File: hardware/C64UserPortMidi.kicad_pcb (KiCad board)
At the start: 2 copper layers, 48 x 47 mm, 13 parts, among them J1 C64-UserPort, J2 MIDI IN DIN-5, J3 AVR-ISP-6, U1 ATtiny13A-PU, U2 6N138, U3 74HC595

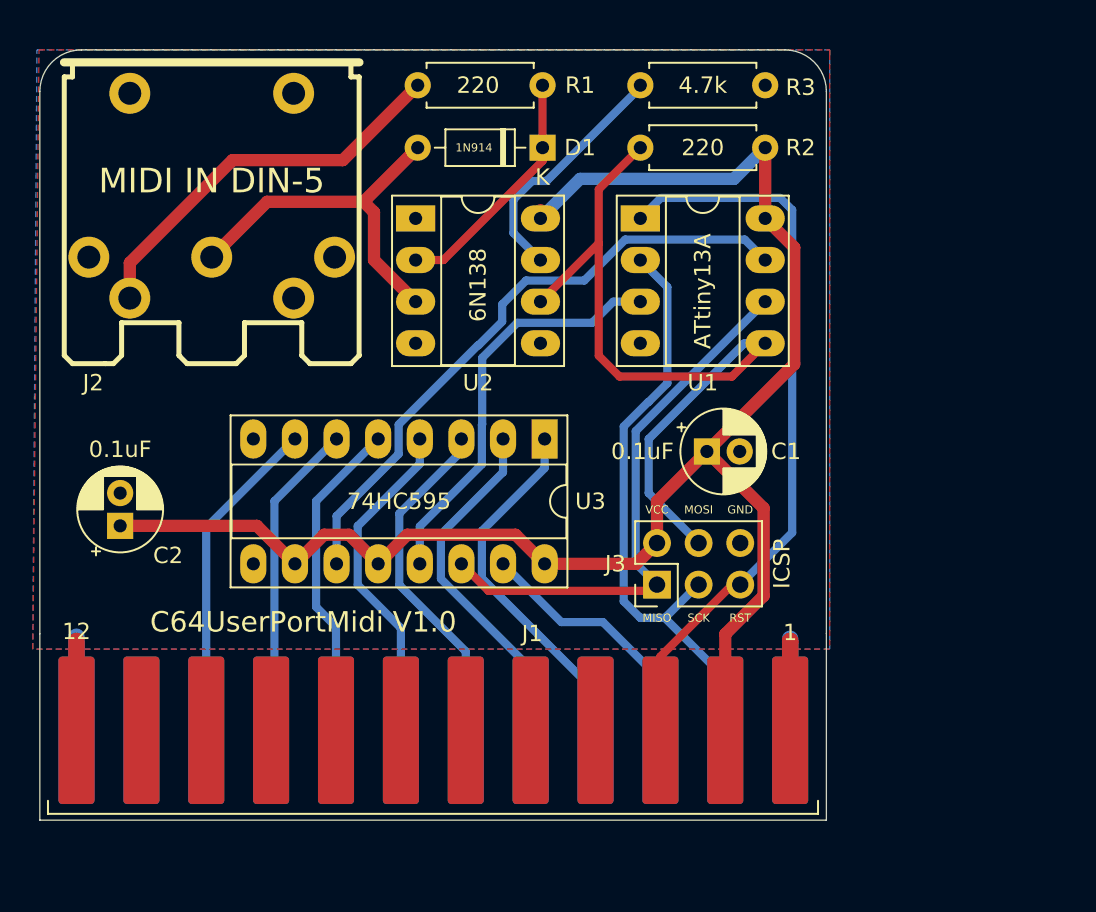
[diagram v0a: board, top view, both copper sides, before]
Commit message: Added data led and latch filtering capacitor to hardware design.
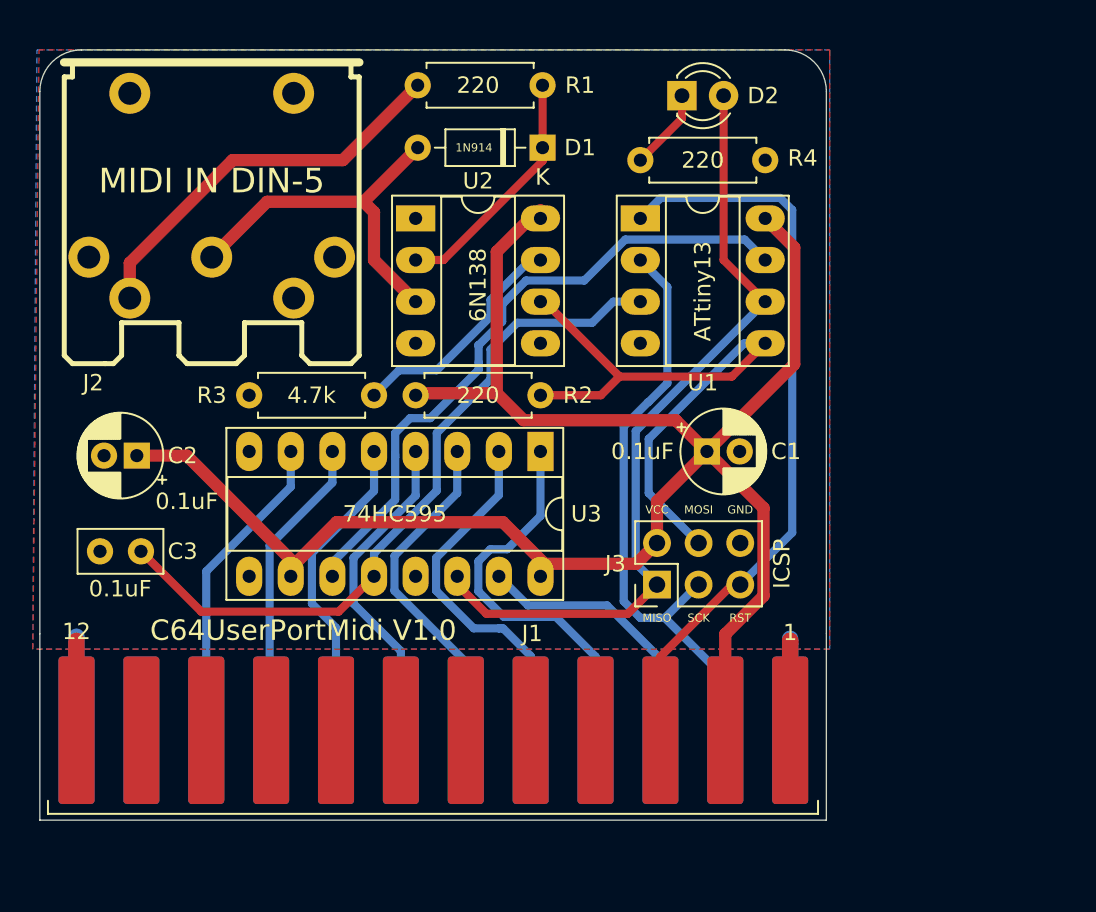
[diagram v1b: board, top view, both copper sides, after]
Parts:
- removed the REF** at (112.3, 110.0)
- added C3: 0.1uF, Capacitor_THT:C_Disc_D5.0mm_W2.5mm_P2.50mm, F.Cu at (113.0, 119.1)
- added D2: LED, LED_THT:LED_D3.0mm, F.Cu at (146.1, 91.3)
- added R4: 220, Resistor_THT:R_Axial_DIN0207_L6.3mm_D2.5mm_P7.62mm_Horizontal, F.Cu at (143.5, 95.2)
- added REF**: OSHW-Logo2_7.3x6mm_SilkScreen, Symbol:OSHW-Logo2_7.3x6mm_SilkScreen, B.Cu at (112.4, 108.8)
- moved R2 26.1 mm to (129.8, 109.6), turned to 0 degrees
- moved R3 24.9 mm to (127.3, 109.6), turned to 180 degrees
- moved C2 4.40 mm to (112.8, 113.3), turned to 180 degrees
- moved U3 0.80 mm to (137.4, 113.0)
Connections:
- net SER renamed DATA
- net SRCLK renamed CLOCK
- U1 pad 3: OE -> LATCH
- U3 pad 12: VCC -> LATCH
- U3 pad 13: OE -> GND
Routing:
- net LATCH: track 0.00 -> 43.8 mm
- net OE: track 25.2 -> 0.00 mm
- net DATA: track 33.9 -> 48.9 mm
- net VCC: track 101.0 -> 112.5 mm
- net RX: track 47.5 -> 38.9 mm
- net Net-(D2-Pad1): track 0.00 -> 4.99 mm
- net CLOCK: track 38.3 -> 40.1 mm
- net /D1: track 22.2 -> 24.0 mm
- net Net-(R3-Pad1): track 15.1 -> 14.2 mm
- net /D7: track 20.0 -> 19.2 mm
- net /D0: track 15.6 -> 16.3 mm
- net /D5: track 19.9 -> 19.2 mm
- net /D4: track 20.6 -> 19.9 mm
- net /D3: track 21.0 -> 20.4 mm
- net /D6: track 19.4 -> 18.9 mm
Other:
- board text added: "ATtiny13"
- board text removed: "ATtiny13A"

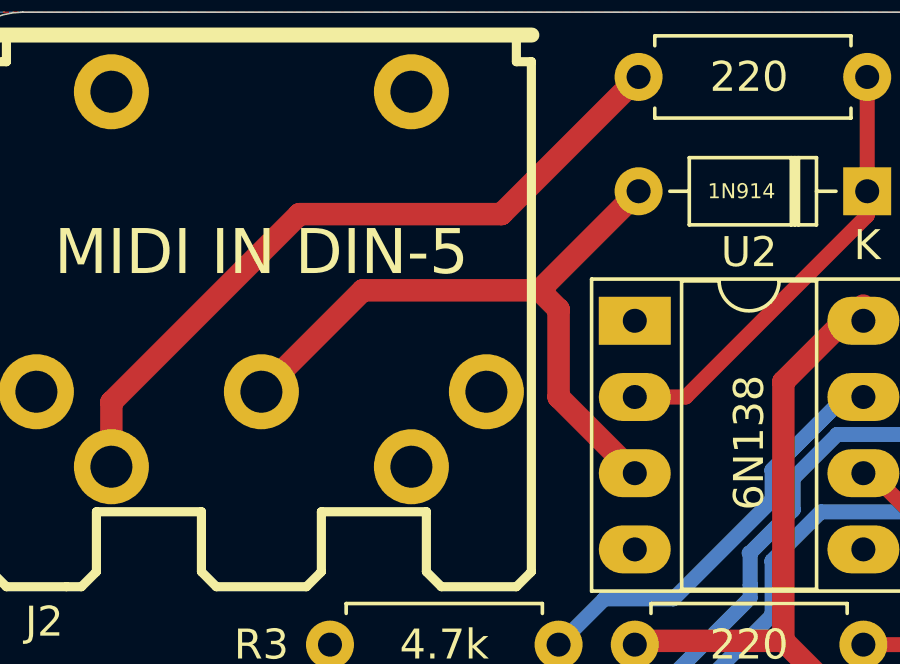
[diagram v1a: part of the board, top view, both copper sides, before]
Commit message: Fixed pin number mixup from schematic symbol to pcb footprint on midi connector.
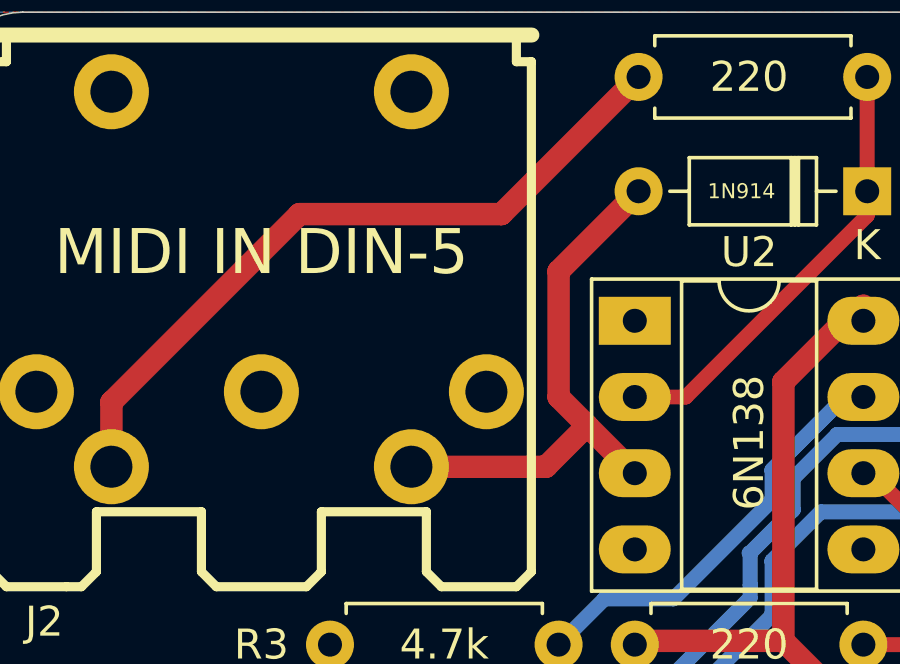
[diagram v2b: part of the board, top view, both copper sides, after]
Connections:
- J2 pad 2: Net-(D1-Pad2) -> Net-(J2-Pad2)
- J2 pad 5: Net-(J2-Pad5) -> Net-(D1-Pad2)
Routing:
- net Net-(D1-Pad2): track 22.8 -> 18.0 mm

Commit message: Updated hardware design files for KiCad 6.0.
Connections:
- net ~RST~ renamed ~{RST}
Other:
- net class Default removed

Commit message: New hardware design update. Version 1.0 Revision A.
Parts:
- removed the REF** at (112.4, 108.8)
- removed U3: 74HC595, Package_DIP:DIP-16_W7.62mm_Socket_LongPads
- added C4: 10uF, Capacitor_THT:CP_Radial_D5.0mm_P2.00mm, F.Cu at (165.5, 127.4)
- added J4: MIDI OUT, Video Connectors:din-5, F.Cu at (153.1, 97.2)
- added JP1: MIDI Output Bypass, Jumper:SolderJumper-2_P1.3mm_Open_RoundedPad1.0x1.5mm, F.Cu at (153.1, 116.5)
- added JP2: RST Bypass, Jumper:SolderJumper-2_P1.3mm_Bridged_RoundedPad1.0x1.5mm, F.Cu at (152.9, 124.0)
- added Q1: 2N3904, Package_TO_SOT_THT:TO-92_Inline, F.Cu at (148.8, 112.4)
- added R5: 220, Resistor_THT:R_Axial_DIN0207_L6.3mm_D2.5mm_P7.62mm_Horizontal, F.Cu at (159.9, 109.2)
- added R6: 220, Resistor_THT:R_Axial_DIN0207_L6.3mm_D2.5mm_P7.62mm_Horizontal, F.Cu at (140.6, 93.9)
- added R7: 10k, Resistor_THT:R_Axial_DIN0207_L6.3mm_D2.5mm_P7.62mm_Horizontal, F.Cu at (159.9, 112.6)
- added REF**: OSHW-Logo_5.7x6mm_SilkScreen, Symbol:OSHW-Logo_5.7x6mm_SilkScreen, F.Cu at (110.4, 95.3)
- added REF**: KiCad-Logo_5mm_SilkScreen, Symbol:KiCad-Logo_5mm_SilkScreen, F.Cu at (165.6, 95.1)
- added REF**: WEEE-Logo_4.2x6mm_SilkScreen, Symbol:WEEE-Logo_4.2x6mm_SilkScreen, B.Cu at (165.4, 95.3)
- added TP1: PD4, TestPoint:TestPoint_THTPad_D1.5mm_Drill0.7mm, F.Cu at (165.7, 122.7)
- added TP3: PD6, TestPoint:TestPoint_THTPad_D1.5mm_Drill0.7mm, F.Cu at (165.7, 119.8)
- added TP4: PA2, TestPoint:TestPoint_THTPad_D1.5mm_Drill0.7mm, F.Cu at (110.6, 123.7)
- C3: footprint Capacitor_THT:C_Disc_D5.0mm_W2.5mm_P2.50mm -> Capacitor_THT:CP_Radial_D5.0mm_P2.00mm
- J2: value MIDI IN DIN-5 -> MIDI IN
- U1: value ATtiny13A-PU -> ATtiny2313-20P; footprint Package_DIP:DIP-8_W7.62mm_Socket_LongPads -> Package_DIP:DIP-20_W7.62mm_Socket_LongPads
- moved C1 39.7 mm to (110.6, 127.4), turned to -90 degrees
- moved C3 31.1 mm to (142.8, 110.3), turned to -90 degrees
- moved U1 30.4 mm to (126.6, 124.1), turned to 90 degrees
- moved C2 26.7 mm to (138.1, 104.7), turned to -90 degrees
- moved U2 23.1 mm to (114.9, 116.5)
- moved D1 21.3 mm to (126.3, 112.6), turned to 0 degrees
- moved R1 18.9 mm to (126.3, 109.2)
- moved J3 15.4 mm to (159.8, 122.8), turned to 180 degrees
- moved R3 11.1 mm to (116.2, 109.2), turned to 0 degrees
- moved J1 8.21 mm to (159.8, 134.0)
- moved R4 8.08 mm to (135.6, 93.9), turned to -90 degrees
- moved D2 8.00 mm to (138.1, 91.3), turned to 90 degrees
- moved R2 6.69 mm to (123.8, 112.6), turned to 180 degrees
- moved J2 5.78 mm to (123.0, 97.2)
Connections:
- C2 pad 1: VCC -> Net-(C2-Pad1)
- C3 pad 1: LATCH -> VCC
- D2 pad 2: DATA -> Net-(D2-Pad2)
- J1 pad 10: Net-(J1-Pad10) -> unconnected-(J1-Pad10)
- J1 pad 11: Net-(J1-Pad11) -> unconnected-(J1-Pad11)
- J1 pad 3: ~{RST} -> Net-(J1-Pad3)
- J1 pad 4: Net-(J1-Pad4) -> unconnected-(J1-Pad4)
- J1 pad 5: Net-(J1-Pad5) -> unconnected-(J1-Pad5)
- J1 pad 6: Net-(J1-Pad6) -> unconnected-(J1-Pad6)
- J1 pad 7: Net-(J1-Pad7) -> unconnected-(J1-Pad7)
- J1 pad 8: Net-(J1-Pad8) -> RECV
- J1 pad 9: Net-(J1-Pad9) -> unconnected-(J1-Pad9)
- J1 pad B: FLAG -> LATCH
- J1 pad J: /D5 -> MOSI
- J1 pad K: /D6 -> MISO
- J1 pad L: /D7 -> SCK
- J2 pad 1: Net-(J2-Pad1) -> unconnected-(J2-Pad1)
- J2 pad 2: Net-(J2-Pad2) -> Net-(C2-Pad1)
- J2 pad 3: Net-(J2-Pad3) -> unconnected-(J2-Pad3)
- J3 pad 1: DATA -> MISO
- J3 pad 3: FLAG -> SCK
- J3 pad 4: RX -> MOSI
- U1 pad 2: FLAG -> RX
- U1 pad 3: LATCH -> TX
- U1 pad 4: GND -> unconnected-(U1-Pad4)
- U1 pad 5: RX -> unconnected-(U1-Pad5)
- U1 pad 6: DATA -> RECV
- U1 pad 7: CLOCK -> Net-(D2-Pad2)
- U1 pad 8: VCC -> Net-(TP1-Pad1)
- U2 pad 1: Net-(U2-Pad1) -> GND
- U2 pad 4: Net-(U2-Pad4) -> GND
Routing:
- net SCK: track 0.00 -> 54.1 mm
- net MISO: track 0.00 -> 49.7 mm
- net DATA: track 48.9 -> 0.00 mm
- net MOSI: track 0.00 -> 43.0 mm
- net CLOCK: track 40.1 -> 0.00 mm
- net Net-(D2-Pad2): track 0.00 -> 38.9 mm
- net FLAG: track 37.4 -> 0.00 mm
- net TX: track 0.00 -> 36.8 mm, vias 0 -> 1
- net LATCH: track 43.8 -> 16.0 mm
- net Net-(TP1-Pad1): track 0.00 -> 23.8 mm, vias 0 -> 1
- net GND: track 22.4 -> 0.00 mm, vias 0 -> 16
- net RX: track 38.9 -> 19.4 mm
- net /D5: track 19.2 -> 0.00 mm
- net Net-(TP3-Pad1): track 0.00 -> 19.2 mm
- net /D7: track 19.2 -> 0.00 mm
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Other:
- board size 48 x 47 mm -> 62.5 x 47.5 mm
- board text added: "10k"
- board text added: "10uF"
- board text added: "2n3904"
- board text added: "ATtiny2313"
- board text added: "C64UserPortMidi V1.0 RevA"
- board text added: "Created By: D Cooper Dalrymple 12-2022 dcdalrymple.com"
- board text removed: "74HC595"
- board text removed: "ATtiny13"
- board text removed: "C64UserPortMidi V1.0"
- board text removed: "Created By: D Cooper Dalrymple 2021 dcdalrymple.com"

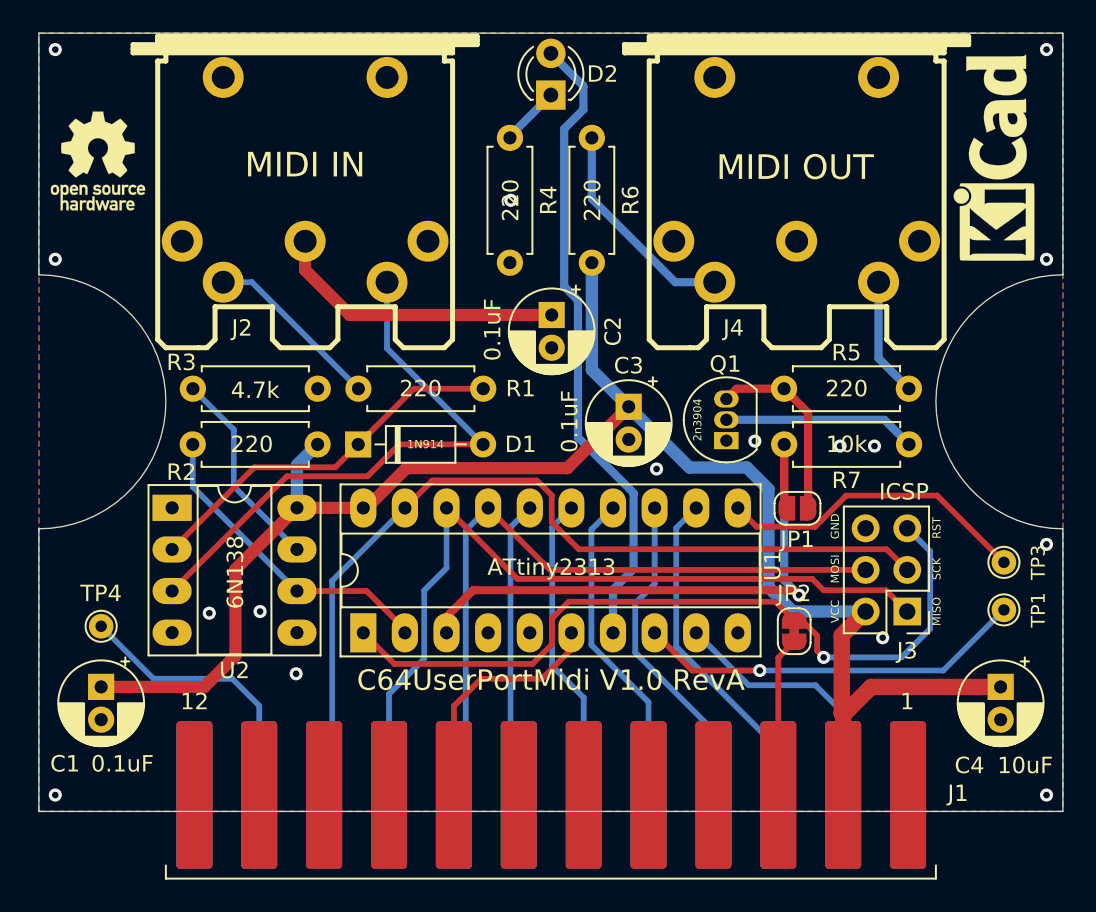
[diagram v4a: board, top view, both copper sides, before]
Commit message: Fixed PA2 error in schematic, rerouted traces, and regenerated gerber files.
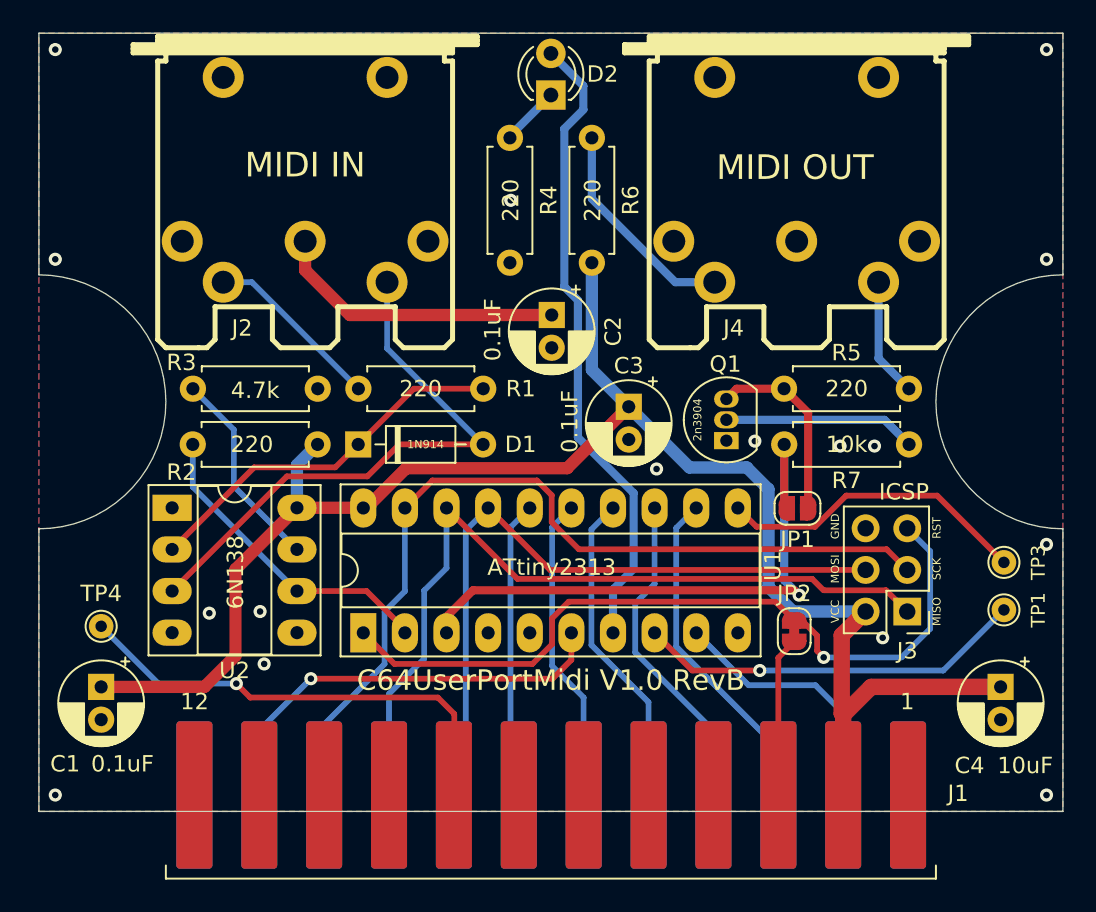
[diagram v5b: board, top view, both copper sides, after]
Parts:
- removed REF**: OSHW-Logo_5.7x6mm_SilkScreen, Symbol:OSHW-Logo_5.7x6mm_SilkScreen
- removed REF**: KiCad-Logo_5mm_SilkScreen, Symbol:KiCad-Logo_5mm_SilkScreen
- removed REF**: WEEE-Logo_4.2x6mm_SilkScreen, Symbol:WEEE-Logo_4.2x6mm_SilkScreen
- TP4: value PA2 -> PC2
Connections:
- net LATCH renamed FLAG
- J1 pad 8: RECV -> Net-(J1-Pad8)
- J1 pad M: Net-(J1-PadM) -> RECV
- TP4 pad 1: Net-(J1-PadM) -> Net-(J1-Pad8)
- U2 pad 1: GND -> unconnected-(U2-Pad1)
- U2 pad 4: GND -> unconnected-(U2-Pad4)
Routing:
- net Net-(J1-Pad8): track 0.00 -> 28.8 mm, vias 0 -> 1
- net Net-(J1-PadM): track 17.1 -> 0.00 mm
- net RECV: track 15.0 -> 26.4 mm, vias 0 -> 1
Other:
- board text added: "C64UserPortMidi V1.0 RevB"
- board text removed: "C64UserPortMidi V1.0 RevA"
